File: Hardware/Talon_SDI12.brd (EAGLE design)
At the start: 140 x 19 mm, 88 parts, among them J1 CONN_TALON_REMOTE, J2 CONN_SDI-12_LOGGERM8_TE_BOARD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, J3 CONN_SDI-12_LOGGERM8_TE_BOARD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, J4 CONN_SDI-12_LOGGERM8_TE_BOARD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, J5 CONN_APOGEE_LOGGER, Q1 AO3419, Q2 2N7002, Q3 AO3419, Q4 2N7002, Q5 AO3419, Q6 2N7002, Q7 AO3419, Q8 2N7002, U1 SN74LVC1G00SC70, U10 SN74LVC1G3157SC70, U11 SN74LVC1G3157SC70, U12 SN74LVC1G3157SC70, U13 SN74LVC1G3157SC70, U14 LM2621, U15 MCP3221, U16 LMR62014SOT23, U17 TXS0102DCU, U18 FDC6330L, U2 SN74LVC2G241DCU, U26 MCP23018QFN, U28 74HC4852, U29 SN74AUP1T157DCK, U3 MAX9034TSSOP, U30 MCP3421A3, U31 PCA9536DFN, U4 INA4180A2, U5 CD4044, U6 SN74HC04, U7 SN74AC08, U8 SIP32431TDFN, U9 SN74LVC1G17DCK

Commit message: Layout and cleanup done, review needed
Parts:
- removed R31: 40.2k, bschulz_passives:R0603
- removed R32: 13.3k, bschulz_passives:R0603
- removed U26: MCP23018QFN, bschulz:QFN24
- removed U28: 74HC4852, bschulz:VQFN-16
- removed U29: SN74AUP1T157DCK, bschulz:DCK_R-PDSO-G6
- removed U30: MCP3421A3, bschulz:SOT23-6L
- removed U31: PCA9536DFN, bschulz:DFN_8_3X3
- added R29: (no value), bschulz_passives:R0603
- added R30: 100k, bschulz_passives:R0402
- added U19, U20: SN74LVC1G3157SC70, bschulz:DCK_R-PDSO-G6
- added U21: SN74LVC1G00SC70, bschulz:DCK_R-PDSO-G5
- added U22: SN74LVC2G241DCU, bschulz:DCU_(R-PDSO-G8)
- added U23: SN74LVC1G17DCK, bschulz:DCK_R-PDSO-G5
- C1: value 0.1uF -> 1uF
- C10, C12, C16: device bschulz_passives:C0603 -> bschulz_passives:C0402
- C11: value 4.7uF -> 0.1uF; device bschulz_passives:C0805 -> bschulz_passives:C0402
- C13: value 10uF -> 0.1uF; device bschulz_passives:C0805 -> bschulz_passives:C0402
- C15: value 220pF -> 10uF; device bschulz_passives:C0603 -> bschulz_passives:C0805
- C2: value 22uF -> 0.1uF; device bschulz_passives:C0805 -> bschulz_passives:C0402
- C3: value 0.1uF -> 22uF; device bschulz_passives:C0603 -> bschulz_passives:C0805
- C4: value (none) -> 0.1uF; device bschulz_passives:C0603 -> bschulz_passives:C0402
- C5: value 68uF -> 4.7uF; device bschulz_passives:C2917 -> bschulz_passives:C0805
- C6: value 0.1uF -> 220pF
- C7: value 1uF -> (none)
- C8: value 0.1uF -> 10uF; device bschulz_passives:C0603 -> bschulz_passives:C0805
- C9: value 10uF -> 68uF; device bschulz_passives:C0805 -> bschulz_passives:C2917
- J1: value CONN_TALON_REMOTE -> CONN_APOGEE_LOGGER; device GEMS_Plugs:1X06_MICROLOCKPLUS -> GEMS_Plugs:1X06_M8_PHOENIX_1456022_BOARDLOCK
- J2: value CONN_SDI-12_LOGGERM8_TE_BOARDLOCK -> CONN_TALON_REMOTE; device GEMS_Plugs:1X03_M8_TE_T40410_BOARDLOCK -> GEMS_Plugs:1X06_MICROLOCKPLUS
- J5: value CONN_APOGEE_LOGGER -> CONN_SDI-12_LOGGERM8_TE_BOARDLOCK; device GEMS_Plugs:1X06_M8_PHOENIX_1456022_BOARDLOCK -> GEMS_Plugs:1X03_M8_TE_T40410_BOARDLOCK
- Q1, Q3: value AO3419 -> 2N7002
- Q6, Q8: value 2N7002 -> AO3419
- R1, R11, R3, R4: device bschulz_passives:R0603 -> bschulz_passives:R0402
- R10: value 82m -> 100k; device bschulz_passives:R0603 -> bschulz_passives:R0402
- R12: value 82m -> 1M; device bschulz_passives:R0603 -> bschulz_passives:R0402
- R13: value 100k -> 470k
- R2: value 82m -> 10k; device bschulz_passives:R0603 -> bschulz_passives:R0402
- R22: value (none) -> 40.2k
- R23: value (none) -> 13.3k
- R24: value 470k -> 115k
- R25: value 115k -> 13.3k
- R26: value 13.3k -> 10k; device bschulz_passives:R0603 -> bschulz_passives:R0402
- R27: value 100k -> 10k; device bschulz_passives:R0603 -> bschulz_passives:R0402
- R28: value 100k -> (none)
- R5: value 1M -> 82m
- R6, R8: value 10k -> 82m
- R9: value 10k -> 100k; device bschulz_passives:R0603 -> bschulz_passives:R0402
- U1: value SN74LVC1G00SC70 -> SN74HC04; device bschulz:DCK_R-PDSO-G5 -> bschulz:TSSOP14
- U10: value SN74LVC1G3157SC70 -> FXMAR2102UMLP; device bschulz:DCK_R-PDSO-G6 -> bschulz:UQFN-8_1.4X1.2
- U11: value SN74LVC1G3157SC70 -> 74HC4852; device bschulz:DCK_R-PDSO-G6 -> bschulz:VQFN-16
- U12: value SN74LVC1G3157SC70 -> SN74AUP1T157DCK
- U13: value SN74LVC1G3157SC70 -> MCP3221; device bschulz:DCK_R-PDSO-G6 -> bschulz:SOT23-5
- U14: value LM2621 -> MCP23018QFN; device bschulz:DGK_S-PDSO-G8 -> bschulz:QFN24
- U15: value MCP3221 -> PCA9536DFN; device bschulz:SOT23-5 -> bschulz:DFN_8_3X3
- U16: value LMR62014SOT23 -> MCP3421A3; device bschulz:DBV0005A -> bschulz:SOT23-6L
- U17: value TXS0102DCU -> SN74LVC1G3157SC70; device bschulz:DCU_(R-PDSO-G8) -> bschulz:DCK_R-PDSO-G6
- U18: value FDC6330L -> SN74LVC1G3157SC70; device bschulz:SOT23-6L -> bschulz:DCK_R-PDSO-G6
- U2: value SN74LVC2G241DCU -> CD4044; device bschulz:DCU_(R-PDSO-G8) -> bschulz:TSSOP16
- U3: value MAX9034TSSOP -> SIP32431TDFN; device bschulz:TSSOP14 -> bschulz:TDFN_4
- U5: value CD4044 -> MAX9034TSSOP; device bschulz:TSSOP16 -> bschulz:TSSOP14
- U6: value SN74HC04 -> SI1869; device bschulz:TSSOP14 -> bschulz:SC-70_6
- U8: value SIP32431TDFN -> LM2621; device bschulz:TDFN_4 -> bschulz:DGK_S-PDSO-G8
- U9: value SN74LVC1G17DCK -> LMR62014SOT23; device bschulz:DCK_R-PDSO-G5 -> bschulz:DBV0005A
- moved R1 108.7 mm to (-53.1, 6.73)
- moved R8 107.2 mm to (53.1, 5.71)
- moved U10 105.2 mm to (47.0, 11.2)
- moved U17 105.2 mm to (-58.2, 7.49), turned to 0 degrees
- moved R28 90.2 mm to (-29.8, 15.1), turned to 270 degrees
- moved R21 88.2 mm to (58.3, 7.75), turned to 90 degrees
- moved U6 84.3 mm to (47.4, 16.5), turned to 90 degrees
- moved R11 78.0 mm to (-53.7, 15.4), turned to 90 degrees
- moved Q5 76.7 mm to (-53.8, 4.19)
- moved R7 76.7 mm to (21.1, 4.57)
- moved Q4 74.9 mm to (58.0, 4.57)
- moved R18 74.2 mm to (-50.5, 8.26), turned to 90 degrees
- moved U18 73.1 mm to (-25.3, 8.51), turned to 0 degrees
- moved R17 72.4 mm to (55.6, 8.26), turned to 0 degrees
- moved R2 72.4 mm to (-19.3, 4.83), turned to 180 degrees
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- renumbered D4 to D3, L3 to L2
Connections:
- net !FAULT1: now also U1.9, U14.24, U2.9; no longer U26.24, U5.9, U6.9
- net !FAULT2: now also U1.3, U14.1, U2.13; no longer U26.1, U5.13, U6.3
- net !FAULT3: now also U1.5, U14.2, U2.10; no longer U26.2, U5.10, U6.5
- net !FAULT4: now also U1.1, U14.3, U2.1; no longer U26.3, U5.1, U6.1
- net !RX: now also U22.6, U23.2; no longer U2.6, U9.2
- net 12V: now also C7.1, C9.+, Q6.2, Q8.2, R10.2, R2.2, R24.2, R3.2, R4.2, U6.4; no longer C4.1, C5.+, Q1.2, Q3.2, R11.2, R25.2, R27.2, R6.2, R9.2, U18.4
- net 3V3: now also C14.1, C16.1, C4.1, C5.1, J2.5, R12.2, R13.2, R26.2, R27.2, R28.2, U1.11, U1.13, U1.14, U10.1, U10.5, U11.16, U12.5, U14.12, U14.8, U15.8, U2.16, U2.5, U21.5, U23.5, U3.3, U8.2, U8.6, U8.7, U9.4; no longer C11.1, C13.1, C2.1, C7.1, J1.5, R22.2, R24.2, R3.2, R4.2, R5.2, U1.5, U14.2, U14.6, U14.7, U16.4, U17.3, U17.6, U26.12, U26.8, U28.16, U29.5, U30.5, U31.8, U5.16, U5.5, U6.11, U6.13, U6.14, U8.3
- net 3V3_SENSE: now also C2.1, R11.2, U3.1, U5.4; no longer C8.1, R8.2, U3.4, U8.1
- net 5V: now also C11.1, C13.1, C8.1, R22.2, U10.8, U13.1, U17.5, U18.5, U19.5, U20.5, U22.8; no longer C14.1, C16.1, C9.1, R31.2, U10.5, U11.5, U12.5, U13.5, U15.1, U17.7, U2.8
- net DATA: now also U17.1, U18.1, U19.1, U20.1, U22.2, U22.3; no longer U10.1, U11.1, U12.1, U13.1, U2.2, U2.3
- net DATA_EN1: now also U14.19, U17.6; no longer U10.6, U26.19
- net DATA_EN2: now also U14.20, U18.6; no longer U11.6, U26.20
- net DATA_EN3: now also U14.21, U19.6; no longer U12.6, U26.21
- net DATA_EN4: now also R30.2, U14.22, U20.6, U6.5; no longer R28.2, U13.6, U18.5, U26.22
- net DATA_OUT1: now also J3.4, U17.4; no longer J2.4, U10.4
- net DATA_OUT2: now also J4.4, U18.4; no longer J3.4, U11.4
- net DATA_OUT3: now also J5.4, U19.4; no longer J4.4, U12.4
- net DATA_OUT4: now also J1.3, U20.4; no longer J5.3, U13.4
- net DATA_SENSE4: now also U20.3; no longer U15.3
- net DIR: now also U14.7, U22.1, U22.7; no longer U2.1, U2.7, U26.7
- net EN1: now also U14.15, U2.6; no longer U26.15, U5.6
- net EN2: now also U14.16, U2.4; no longer U26.16, U5.4
- net EN3: now also U14.17, U2.12; no longer U26.17, U5.12
- net EN4: now also U14.18, U2.14; no longer U26.18, U5.14
- net FAULT1: now also U1.8; no longer U6.8
- net FAULT2: now also U1.4; no longer U6.4
- net FAULT3: now also U1.6; no longer U6.6
- net FAULT4: now also U1.2; no longer U6.2
- net FOUT: now also U14.6, U21.1; no longer U1.1, U26.6
- net GND: now also C15.2, C3.2, C5.2, C9.-, J1.1, J2.6, J5.3, Q1.2, Q3.2, R18.1, R20.1, R25.1, R29.1, R30.1, R9.1, U1.7, U10.4, U11.8, U11.EP, U14.23, U14.EP, U15.4, U15.EP, U16.6, U18.2, U19.2, U2.8, U20.2, U21.3, U22.4, U23.3, U3.2, U3.EP, U5.11, U6.1, U8.1, U8.5, U9.2; no longer C5.-, C6.2, C7.2, C9.2, J2.3, J5.1, J5.6, Q6.2, Q8.2, R13.1, R15.1, R17.1, R26.1, R28.1, R32.1, U1.3, U10.2, U11.2, U14.1, U14.5, U15.2, U18.1, U2.4, U26.23, U26.EP, U28.8, U28.EP, U29.2, U3.11, U30.2, U30.6, U31.4, U31.EP, U5.8, U6.7, U8.2, U8.EP, U9.3
- net LATCH1: now also U2.7, U5.1; no longer U3.1, U5.7
- net LATCH2: now also U2.3, U5.7; no longer U3.7, U5.3
- net LATCH3: now also U2.11, U5.8; no longer U3.8, U5.11
- net LATCH4: now also U2.15, U5.14; no longer U3.14, U5.15
- net MOS_CTRL1: now also Q1.1; no longer Q2.1
- net MOS_CTRL2: now also Q2.1; no longer Q4.1
- net MOS_CTRL3: now also Q3.1; no longer Q6.1
- net MOS_CTRL4: now also Q4.1; no longer Q8.1
- net MUX_EN: now also U11.6, U15.5; no longer U28.6, U31.5
- net MUX_SEL0: now also U11.10, U15.1; no longer U28.10, U31.1
- net MUX_SEL1: now also U11.9, U15.2; no longer U28.9, U31.2
- net MUX_SEL2: now also U12.4, U15.3; no longer U29.4, U31.3
- net N$1: now also Q2.3, Q6.1, R2.1; no longer Q3.1, Q4.3, R9.1
- net N$10: now also C6.2, R22.1, R23.2, U9.3; no longer C15.2, R31.1, R32.2, U16.3
- net N$11: now also R10.1, U6.6; no longer R27.1, U18.6
- net N$14: now also R28.1, R29.2, U14.11; no longer R21.2, R22.1, U26.11
- net N$18: now also U11.3, U12.3; no longer U28.3, U29.3
- net N$2: now also Q1.3, Q5.1, R1.1; no longer Q1.1, Q2.3, R6.1
- net N$3: now also Q3.3, Q7.1, R3.1; no longer Q5.1, Q6.3, R11.1
- net N$38: now also U11.13, U12.1; no longer U28.13, U29.1
- net N$4: now also Q4.3, Q8.1, R4.1; no longer Q7.1, Q8.3, R1.1
- net N$5: now also U21.4, U22.5; no longer U1.4, U2.5
- net N$7: now also C4.2, R13.1, U8.3; no longer C3.2, R24.1, U14.3
- net N$8: now also U8.8; no longer U14.8
- net N$9: now also C7.2, R24.1, R25.2, U8.4; no longer C4.2, R25.1, R26.2, U14.4
- net POS_DETECT: now also R12.1, U14.4; no longer R5.1, U26.4
- net RX: now also J2.1, U23.4; no longer J1.1, U9.4
- net SCL: now also J2.3, R27.1, U10.3, U14.9, U15.6, U16.3; no longer J1.3, R4.1, U17.4, U26.9, U30.3, U31.6
- net SCL_HV: now also U10.6, U13.5; no longer U15.5, U17.1
- net SDA: now also J2.4, R26.1, U10.2, U14.10, U15.7, U16.4; no longer J1.4, R3.1, U17.5, U26.10, U30.4, U31.7
- net SDA_HV: now also U10.7, U13.4; no longer U15.4, U17.8
- net SENSE1: now also U11.12, U5.2; no longer U28.12, U3.2
- net SENSE1+: now also Q5.3, R5.1; no longer Q1.3, R7.1
- net SENSE2: now also U11.14, U5.6; no longer U28.14, U3.6
- net SENSE2+: now also Q6.3, R6.1; no longer Q3.3, R10.1
- net SENSE3: now also U11.15, U5.9; no longer U28.15, U3.9
- net SENSE3+: now also Q7.3, R7.1; no longer Q5.3, R12.1
- net SENSE4: now also U11.11, U5.13; no longer U28.11, U3.13
- net SENSE4+: now also Q8.3, R8.1; no longer Q7.3, R2.1
- net SENSE_EN: now also R9.2, U14.5, U3.4; no longer R13.2, U26.5, U8.4
- net SW1: now also U9.1; no longer U16.1
- net SWITCHED_SENSE: now also U12.6, U16.1; no longer U29.6, U30.1
- net TX: now also J2.2, U21.2; no longer J1.2, U1.2
- net VHEATER: now also J1.5, U6.2, U6.3; no longer J5.5, U18.2, U18.3
- net VPORT1_OUT: now also J3.1, R5.2; no longer J2.1, R7.2
- net VPORT1_OUT_SENSE: now also R18.2, U11.1; no longer R15.2, U28.1
- net VPORT2_OUT: now also J4.1, R15.1, R6.2; no longer J3.1, R10.2, R16.1
- net VPORT2_OUT_SENSE: now also R15.2, R19.2, U11.5; no longer R16.2, R17.2, U28.5
- net VPORT3_OUT: now also J5.1, R16.1, R7.2; no longer J4.1, R12.2, R18.1
- net VPORT3_OUT_SENSE: now also R16.2, R20.2, U11.2; no longer R18.2, R19.2, U28.2
- net VPORT4_OUT: now also J1.2, R17.1, R8.2; no longer J5.2, R2.2, R20.1
- net VPORT4_OUT_SENSE: now also R17.2, R21.2, U11.4; no longer R20.2, R23.2, U28.4
- net VREF: now also R11.1, U5.10, U5.12, U5.3, U5.5; no longer R8.1, U3.10, U3.12, U3.3, U3.5
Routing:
- net GND: track 375.7 -> 396.9 mm
- net 5V: track 187.7 -> 197.6 mm
- net 3V3: track 210.9 -> 214.8 mm
- net 12V: track 160.8 -> 162.6 mm
- net SDA: track 103.1 -> 104.9 mm
- net SDA_HV: track 15.5 -> 14.1 mm
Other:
- board text added: "Port1"
- board text added: "Port2"
- board text added: "Port3"
- board text added: "Port4"
- board text added: "Talon - SDI-12 v0.0 Bobby Schulz"

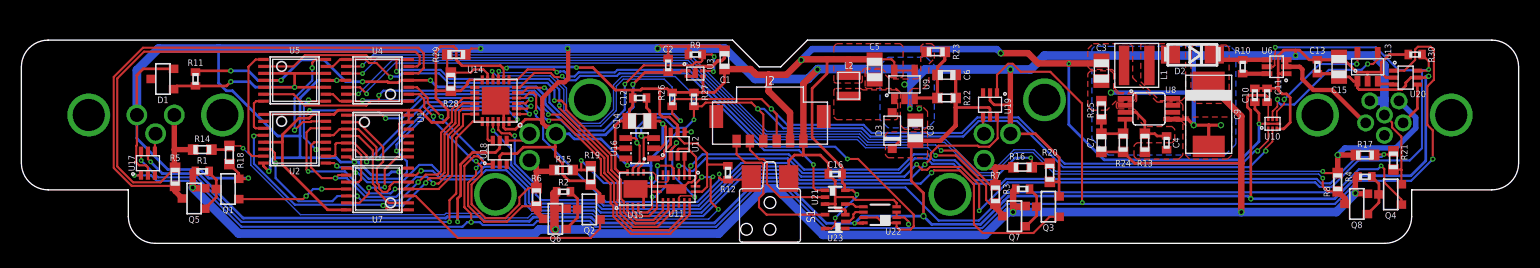
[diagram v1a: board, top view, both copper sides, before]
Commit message: Layout, gerbers, and BoM for v0.0 - submitted to fab
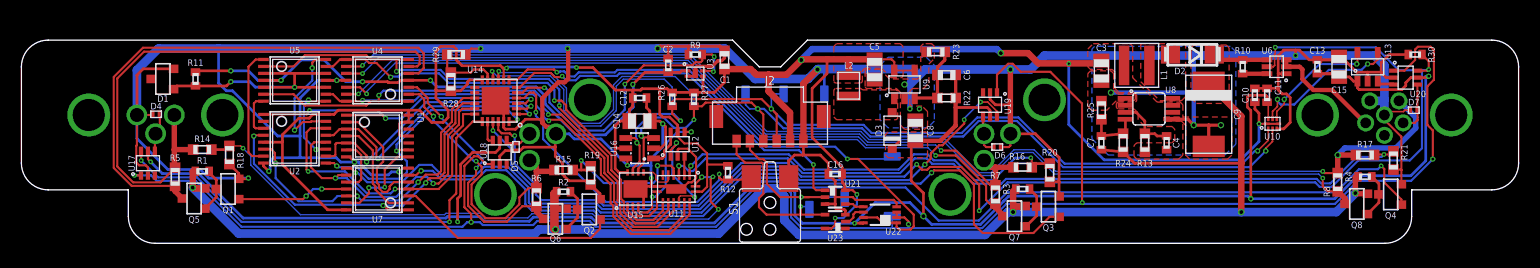
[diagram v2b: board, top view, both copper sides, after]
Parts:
- added D4, D5, D6, D7: 6V, bschulz:D0402
- added TP1, TP2, TP3, TP4, TP5, TP6, TP7: TESTPOINTRCU, bschulz:TESTPOINT_0603
- C7: value (none) -> 39pF; device bschulz_passives:C0603 -> bschulz_passives:C0402
- R14, R15, R16, R17: value (none) -> 499k
- R18, R19, R20, R21: value (none) -> 100k
- R28: value (none) -> 110k
- R29: value (none) -> 49.9k
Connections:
- net DATA: now also TP4.1
- net DATA_OUT1: now also D4.2
- net DATA_OUT2: now also D5.2
- net DATA_OUT3: now also D6.2
- net DATA_OUT4: now also D7.2
- net DIR: now also TP5.1
- net GND: now also D4.1, D5.1, D6.1, D7.1, TP1.1
- net RX: now also TP3.1
- net SCL: now also TP7.1
- net SDA: now also TP6.1
- net TX: now also TP2.1
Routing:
- net GND: track 396.9 -> 405.3 mm
- net TX: track 10.8 -> 15.7 mm, vias 0 -> 1
- net DIR: track 51.1 -> 55.3 mm
- net DATA: track 179.2 -> 181.7 mm
- net SDA: track 104.9 -> 107.2 mm
- net SCL: track 104.9 -> 107.2 mm
- net 5V: track 197.6 -> 199.9 mm
- net DATA_OUT3: track 1.65 -> 3.66 mm
- net DATA_OUT1: track 1.68 -> 3.66 mm
- net RX: track 14.8 -> 16.5 mm, vias 0 -> 1
- net 12V: track 162.6 -> 164.0 mm
- net DATA_OUT2: track 2.78 -> 3.94 mm
- net DATA_OUT4: track 4.14 -> 4.78 mm
- net DATA_EN3: track 59.0 -> 59.4 mm, vias 2 -> 4
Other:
- board text added: "DATA"
- board text added: "DIR"
- board text added: "GND"
- board text added: "RX"
- board text added: "SCL"
- board text added: "SDA"
- board text added: "SN"
- board text added: "TX"

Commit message: V0.1 Updates - Added EEPROM
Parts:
- added U24: 24AA02SOT23, bschulz:SOT23-5
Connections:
- net 3V3: now also U24.4
- net GND: now also U24.2, U24.5
- net SCL: now also U24.1
- net SDA: now also U24.3
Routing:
- net GND: track 405.3 -> 410.2 mm
- net SCL: track 107.2 -> 112.0 mm, vias 5 -> 6
- net 3V3: track 215.3 -> 218.1 mm
- net SDA: track 107.2 -> 109.0 mm, vias 5 -> 6
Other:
- board text added: "Talon - SDI-12 v0.1 Bobby Schulz"
- board text removed: "Talon - SDI-12 v0.0 Bobby Schulz"

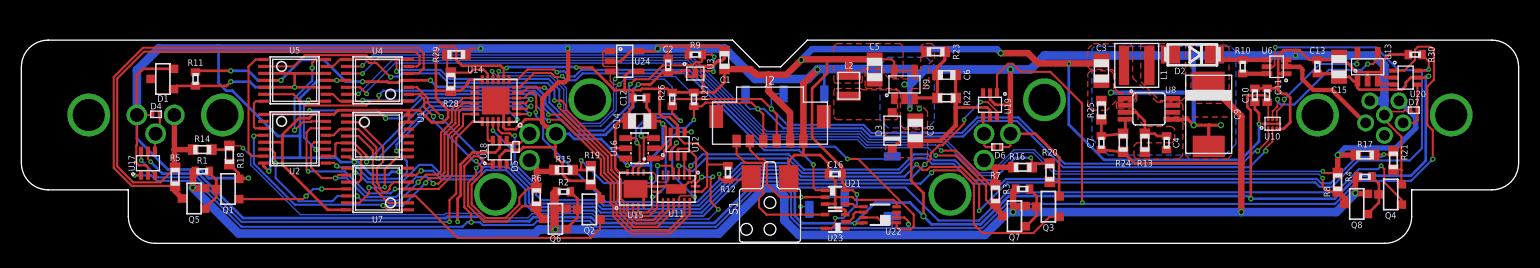
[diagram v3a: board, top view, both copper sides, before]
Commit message: Updated v1.0, sent to fab
Made fixes for v1.0:
- Fixed bypass control
- Changed arrangement of 12V reg
- Added filter lines (clitch protection) to sense lines
- Flipped Talon connector port pinout
- Adjusted port 4 topology to deal with pulldown issue
- Moved MUX (U11/U15) to prevent soldering issues 
- Moved U7 to prevent bumping 
- Added additional protection circuitry on SDI-12 outputs
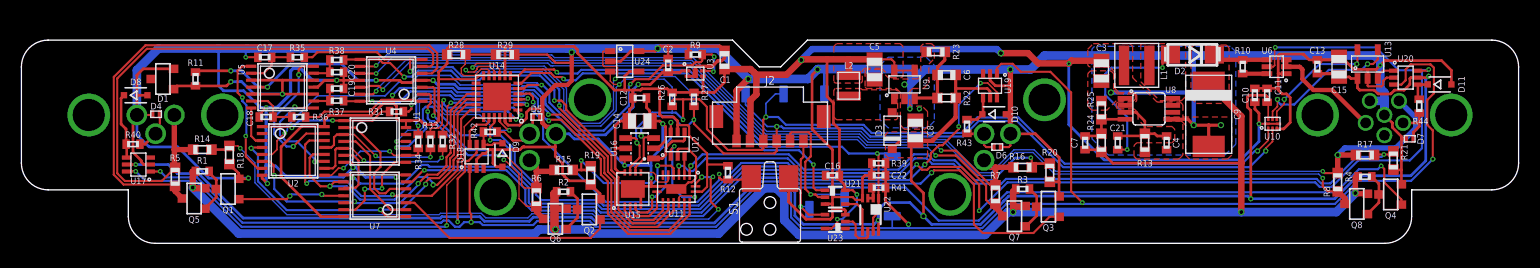
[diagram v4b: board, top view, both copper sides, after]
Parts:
- removed R30: 100k, bschulz_passives:R0402
- added C17, C18, C19, C20: 0.1uF, bschulz_passives:C0402
- added C21: (no value), bschulz_passives:C0402
- added C22: 3.3nF, bschulz_passives:C0402
- added D10, D11, D8, D9: (no value), bschulz:SOD323-R
- added R31, R32, R33, R34, R35, R36, R37, R38: 1k, bschulz_passives:R0402
- added R39: 200K, bschulz_passives:R0402
- added R40, R41, R42, R43, R44: 510R, bschulz_passives:R0402
- U12: value SN74AUP1T157DCK -> SN74LVC1G3157SC70
- moved R29 4.57 mm to (-24.8, 17.7)
- moved D5 3.38 mm to (-21.8, 11.8), turned to 180 degrees
- moved D7 2.69 mm to (59.8, 9.78)
- moved R28 2.59 mm to (-29.3, 17.7), turned to 180 degrees
- moved U18 2.19 mm to (-27.4, 8.13)
- moved R24 2.03 mm to (31.0, 9.40)
- moved U19 1.78 mm to (20.6, 14.7)
- moved C7 1.52 mm to (29.5, 9.40)
- moved U5 1.31 mm to (-45.6, 14.6)
- moved U4 1.27 mm to (-35.4, 15.2)
- moved U2 1.15 mm to (-44.6, 8.64)
- moved U17 0.90 mm to (-59.1, 7.37), turned to 90 degrees
- moved U22 0.89 mm to (9.40, 2.67), turned to 180 degrees
- moved U7 0.68 mm to (-37.0, 4.45)
- moved U1 0.57 mm to (-37.0, 9.53)
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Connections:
- new net !DATA_EN4: U1.10, U20.6, U6.5
- new net DATA_OUT_PROTEC1: D8.C, R40.2, U17.4
- new net DATA_OUT_PROTEC2: D9.C, R42.2, U18.4
- new net DATA_OUT_PROTEC3: D10.C, R43.2, U19.4
- new net DATA_OUT_PROTEC4: D11.C, R44.2, U20.4
- new net DATA_PROTEC: R41.2, U22.2, U22.3
- new net FAULT1_SENSE: R34.1, U14.24
- new net FAULT2_SENSE: R33.1, U14.1
- new net FAULT3_SENSE: R32.1, U14.2
- new net FAULT4_SENSE: R31.1, U14.3
- new net SENSE1_FILT: C17.1, R35.2, U5.2
- new net SENSE2_FILT: C18.1, R36.2, U5.6
- new net SENSE3_FILT: C19.1, R37.2, U5.9
- new net SENSE4_FILT: C20.1, R38.2, U5.13
- net !FAULT1: now also U1.8, U7.13; no longer U1.9, U14.24, U2.9
- net !FAULT2: now also U1.4, U7.2; no longer U1.3, U14.1, U2.13
- net !FAULT3: now also U1.6, U7.10; no longer U1.5, U14.2, U2.10
- net !FAULT4: now also U1.2, U7.5; no longer U1.1, U14.3, U2.1
- net 3V3: now also J2.2; no longer J2.5, U1.11, U2.5
- net DATA: now also C22.1, R39.2, R41.1, U20.3; no longer U20.1, U22.2, U22.3
- net DATA_EN4: now also U1.11; no longer R30.2, U20.6, U6.5
- net DATA_OUT1: now also R40.1; no longer U17.4
- net DATA_OUT2: now also R42.1; no longer U18.4
- net DATA_OUT3: now also R43.1; no longer U19.4
- net DATA_OUT4: now also R44.1; no longer U20.4
- net DATA_SENSE4: now also U20.1; no longer U20.3
- net FAULT1: now also R34.2, U1.9, U2.9; no longer U1.8, U7.13
- net FAULT2: now also R33.2, U1.3, U2.13; no longer U1.4, U7.2
- net FAULT3: now also R32.2, U1.5, U2.10; no longer U1.6, U7.10
- net FAULT4: now also R31.2, U1.1, U2.1; no longer U1.2, U7.5
- net GND: now also C17.2, C18.2, C19.2, C20.2, C22.2, D10.A, D11.A, D8.A, D9.A, J2.1, R39.1; no longer J2.6, R30.1
- net MUX_SEL2: now also U12.6; no longer U12.4
- net N$7: now also C21.2
- net N$8: now also C21.1
- net RX: now also J2.6; no longer J2.1
- net SCL: now also J2.4; no longer J2.3
- net SDA: now also J2.3; no longer J2.4
- net SENSE1: now also R35.1; no longer U5.2
- net SENSE2: now also R36.1; no longer U5.6
- net SENSE3: now also R37.1; no longer U5.9
- net SENSE4: now also R38.1; no longer U5.13
- net SENSE_EN: now also U2.5
- net SWITCHED_SENSE: now also U12.4; no longer U12.6
- net TX: now also J2.5; no longer J2.2
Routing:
- net !DATA_EN4: track 0.00 -> 140.1 mm, vias 0 -> 5
- net DATA_EN4: track 129.3 -> 17.5 mm, vias 5 -> 2
- net GND: track 410.2 -> 446.9 mm, vias 20 -> 22
- net SENSE_EN: track 27.8 -> 58.2 mm, vias 4 -> 5
- net !FAULT4: track 31.7 -> 11.3 mm, vias 3 -> 0
- net !FAULT3: track 25.3 -> 5.42 mm, vias 2 -> 0
- net !FAULT1: track 26.5 -> 9.03 mm, vias 3 -> 2
- net N$8: track 0.00 -> 16.0 mm, vias 0 -> 2
- net !FAULT2: track 24.7 -> 10.3 mm, vias 2 -> 0
- net FAULT1_SENSE: track 0.00 -> 14.0 mm, vias 0 -> 2
- net FAULT4_SENSE: track 0.00 -> 13.9 mm, vias 0 -> 2
- net FAULT2_SENSE: track 0.00 -> 12.9 mm, vias 0 -> 2
- net FAULT3_SENSE: track 0.00 -> 11.3 mm, vias 0 -> 2
- net SDA: track 109.0 -> 118.1 mm
- net FAULT3: track 5.38 -> 14.4 mm, vias 0 -> 2
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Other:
- board text added: "Talon - SDI-12 v1.0 Bobby Schulz"
- board text removed: "Talon - SDI-12 v0.1 Bobby Schulz"
